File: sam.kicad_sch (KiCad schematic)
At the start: 57 parts, among them IC1 HYB4116, IC15 MC6883, IC16 74LS244, IC2 HYB4116, IC3 HYB4116, IC31 74LS02, IC33 74LS138, IC4 HYB4116, IC5 HYB4116, IC6 HYB4116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

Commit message: validate component values
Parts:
- removed C10, C11, C37: 4.7uF, Capacitor_THT:C_Disc_D3.0mm_W2.0mm_P2.50mm, symbol Device:C_Small
- removed C13: 10uF, Capacitor_THT:C_Disc_D3.0mm_W2.0mm_P2.50mm, symbol Device:C_Small
- added C10, C11, C37: 4.7uF, Capacitor_THT:CP_Radial_D5.0mm_P2.50mm, symbol Device:C_Polarized_Small
- added C13: 10uF, Capacitor_THT:CP_Radial_D5.0mm_P2.50mm, symbol Device:C_Polarized_Small
- C12, C14, C15, C16, C17, C18, C19, C20, C21: footprint Capacitor_THT:C_Disc_D3.0mm_W2.0mm_P2.50mm -> Capacitor_THT:C_Disc_D4.3mm_W1.9mm_P5.00mm
- C50, C51, C52, C53, C54, C55, C56, C57: footprint Capacitor_THT:C_Disc_D3.0mm_W2.0mm_P2.50mm -> Capacitor_THT:C_Disc_D4.7mm_W2.5mm_P5.00mm
- C58: value 0.1uF -> 0.01uF; footprint Capacitor_THT:C_Disc_D3.0mm_W2.0mm_P2.50mm -> Capacitor_THT:C_Disc_D4.3mm_W1.9mm_P5.00mm
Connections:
- net +5V: now also C13.1, C37.1
- net -5V: now also C10.2
- net GND: now also C10.1, C11.2, C13.2, C37.2
- net RAM VDD: now also C11.1

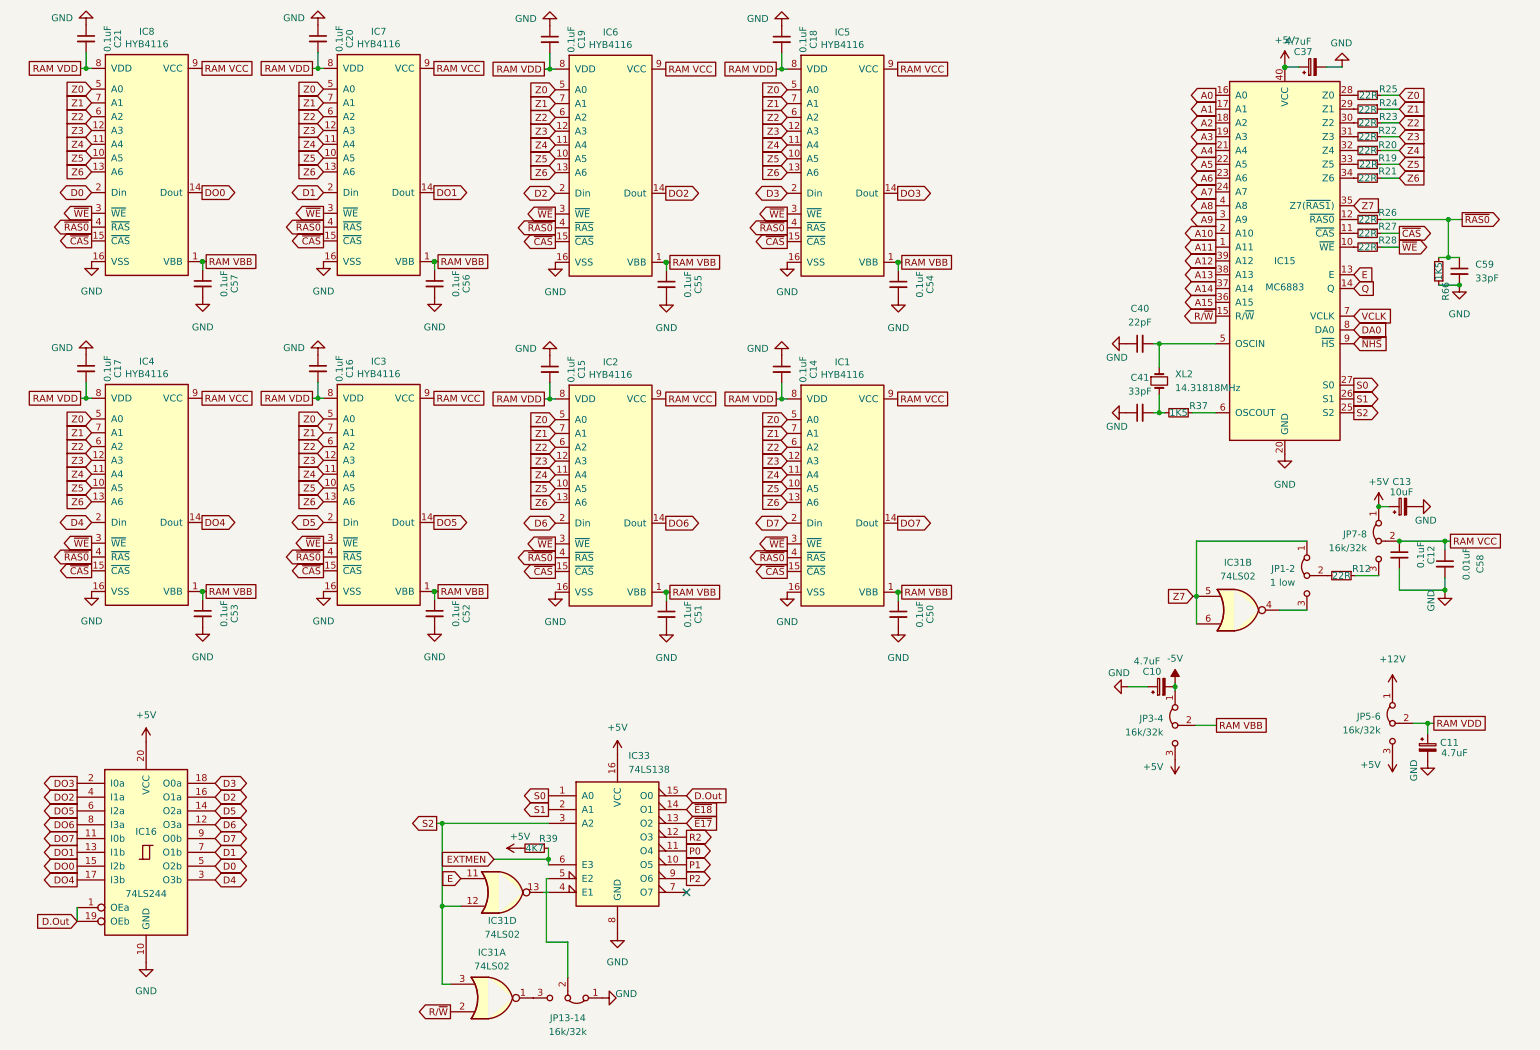
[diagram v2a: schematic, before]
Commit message: cross-reference items to suppliers
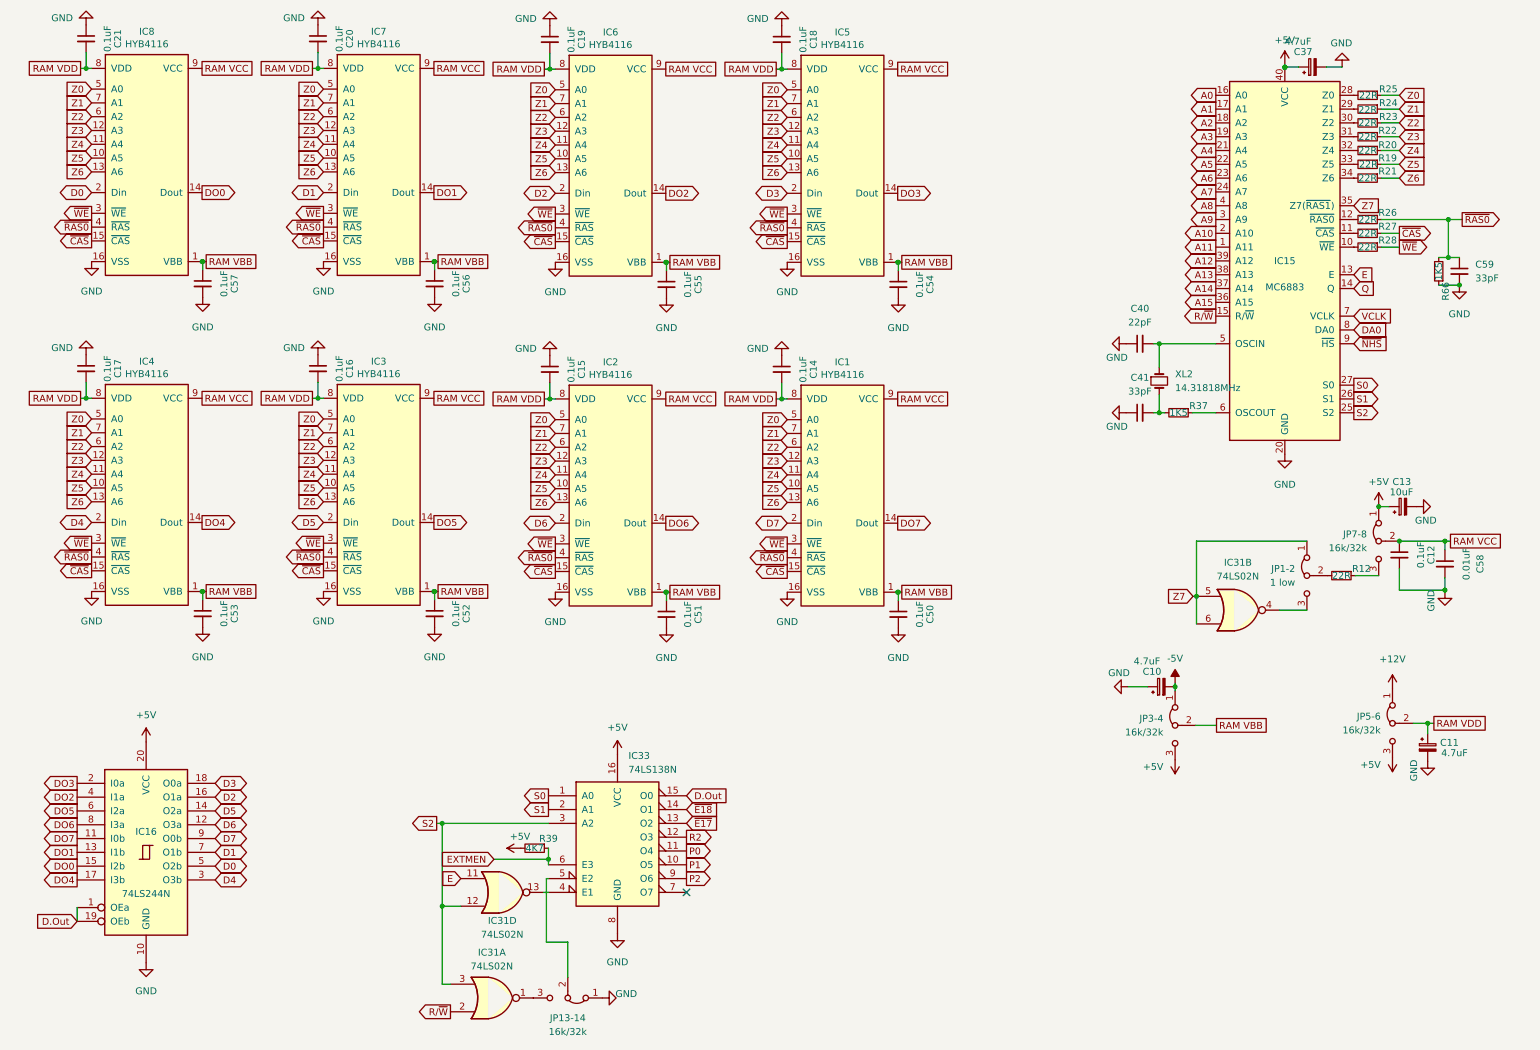
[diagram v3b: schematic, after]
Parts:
- IC16: value 74LS244 -> 74LS244N
- IC31: value 74LS02 -> 74LS02N
- IC33: value 74LS138 -> 74LS138N; DigiKey (none) -> 296-1639-5-ND
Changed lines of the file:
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@@
     (in_bom yes) (on_board yes)
     (property "Reference" "IC16" (id 0) (at 35.306 165.1 0))
-    (property "Value" "74LS244" (id 1) (at 35.306 176.53 0))
+    (property "Value" "74LS244N" (id 1) (at 35.306 176.53 0))
     (property "Footprint" "Package_DIP:DIP-20_W7.62mm" (id 2) (at 35.306 168.91 0)
       (effects (font (size 1.27 1.27)) hide)
@@
     (in_bom yes) (on_board yes)
     (property "Reference" "IC31" (id 0) (at 100.838 181.483 0))
-    (property "Value" "74LS02" (id 1) (at 100.838 184.023 0))
+    (property "Value" "74LS02N" (id 1) (at 100.838 184.023 0))
     (property "Footprint" "Package_DIP:DIP-14_W7.62mm" (id 2) (at 100.838 176.276 0)
       (effects (font (size 1.27 1.27)) hide)
@@
       (effects (font (size 1.27 1.27)) (justify left))
     )
-    (property "Value" "74LS138" (id 1) (at 124.0664 153.67 0)
+    (property "Value" "74LS138N" (id 1) (at 124.0664 153.67 0)
       (effects (font (size 1.27 1.27)) (justify left))
     )
@@
     )
     (property "Datasheet" "http://www.ti.com/lit/gpn/sn74LS138" (id 3) (at 122.047 166.116 0)
+      (effects (font (size 1.27 1.27)) hide)
+    )
+    (property "DigiKey" "296-1639-5-ND" (id 4) (at 122.047 166.116 0)
       (effects (font (size 1.27 1.27)) hide)
     )
@@
     (in_bom yes) (on_board yes) (fields_autoplaced)
     (property "Reference" "IC31" (id 0) (at 236.22 115.57 0))
-    (property "Value" "74LS02" (id 1) (at 236.22 118.11 0))
+    (property "Value" "74LS02N" (id 1) (at 236.22 118.11 0))
     (property "Footprint" "Package_DIP:DIP-14_W7.62mm" (id 2) (at 236.22 124.333 0)
       (effects (font (size 1.27 1.27)) hide)
@@
     (in_bom yes) (on_board yes) (fields_autoplaced)
     (property "Reference" "IC31" (id 0) (at 98.933 187.325 0))
-    (property "Value" "74LS02" (id 1) (at 98.933 189.865 0))
+    (property "Value" "74LS02N" (id 1) (at 98.933 189.865 0))
     (property "Footprint" "Package_DIP:DIP-14_W7.62mm" (id 2) (at 98.933 195.707 0)
       (effects (font (size 1.27 1.27)) hide)

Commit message: update part numbers
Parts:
- C12, C14, C15, C16, C17, C18, C19, C20, C21: DigiKey (none) -> BC1101CT-ND
- C13: DigiKey 399-ESK106M016AC3KACT-ND -> 732-8593-1-ND
- C40: DigiKey (none) -> 399-13930-1-ND
- C41, C59: DigiKey (none) -> BC1007CT-ND
- C50, C51, C52, C53, C54, C55, C56, C57: footprint Capacitor_THT:C_Disc_D4.7mm_W2.5mm_P5.00mm -> Capacitor_THT:C_Disc_D4.3mm_W1.9mm_P5.00mm; DigiKey (none) -> BC1101CT-ND
- C58: DigiKey (none) -> BC2662CT-ND
- IC1, IC2, IC3, IC4, IC5, IC6, IC7, IC8: Note (none) -> use general 4164 with suitable timing
- IC15: Note (none) -> donor
- IC16: DigiKey (none) -> 296-1653-5-ND
- IC31: DigiKey (none) -> 296-1627-5-ND
- XL2: footprint Crystal:Crystal_HC18-U_Horizontal -> Crystal:Crystal_HC49-U_Horizontal; DigiKey (none) -> CTX088-ND

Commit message: resolve part numbers
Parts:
- JP1-2: DigiKey (none) -> 952-2521-ND
- R12, R19, R20, R21, R22, R23, R24, R25, R26, R27, R28: DigiKey (none) -> CF14JT22R0CT-ND
- R37, R66: DigiKey (none) -> CF14JT1K50CT-ND
- R39: DigiKey (none) -> CF14JT4K70CT-ND
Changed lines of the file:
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@@
+      (effects (font (size 1.27 1.27)) hide)
+    )
+    (property "DigiKey" "CF14JT22R0CT-ND" (id 4) (at 260.096 42.291 0)
       (effects (font (size 1.27 1.27)) hide)
     )
@@
       (effects (font (size 1.27 1.27)) hide)
     )
+    (property "DigiKey" "CF14JT22R0CT-ND" (id 4) (at 260.096 54.991 0)
+      (effects (font (size 1.27 1.27)) hide)
+    )
     (pin "1")
     (pin "2")
@@
       (effects (font (size 1.27 1.27)) hide)
     )
+    (pin "1")
+    (pin "2")
+    (pin "3")
+    (pin "4")
+    (pin "5")
+    (pin "6")
+    (pin "10")
+    (pin "8")
+    (pin "9")
     (pin "11")
     (pin "12")
     (pin "13")
+    (pin "14")
+    (pin "7")
   )
   (symbol (lib_id "power:GND") (at 88.392 127.508 0) (unit 1)
@@
       (effects (font (size 1.27 1.27)) hide)
     )
+    (property "DigiKey" "CF14JT1K50CT-ND" (id 4) (at 225.298 88.011 0)
+      (effects (font (size 1.27 1.27)) hide)
+    )
     (pin "1")
     (pin "2")
@@
       (effects (font (size 1.27 1.27)) hide)
     )
+    (pin "1")
+    (pin "2")
+    (pin "3")
     (pin "4")
     (pin "5")
     (pin "6")
+    (pin "10")
+    (pin "8")
+    (pin "9")
+    (pin "11")
+    (pin "12")
+    (pin "13")
+    (pin "14")
+    (pin "7")
   )
   (symbol (lib_id "power:GND") (at 216.027 138.43 270) (mirror x) (unit 1)
@@
       (effects (font (size 1.27 1.27)) hide)
     )
+    (property "DigiKey" "CF14JT4K70CT-ND" (id 4) (at 106.807 168.148 0)
+      (effects (font (size 1.27 1.27)) hide)
+    )
     (pin "1")
     (pin "2")
@@
     (pin "2")
     (pin "3")
+    (pin "4")
+    (pin "5")
+    (pin "6")
+    (pin "10")
+    (pin "8")
+    (pin "9")
+    (pin "11")
+    (pin "12")
+    (pin "13")
+    (pin "14")
+    (pin "7")
   )
   (symbol (lib_id "Memory_RAM_Siemens:HYB4116") (at 120.777 103.251 0) (unit 1)
@@
       (effects (font (size 1.27 1.27)) hide)
     )
+    (property "DigiKey" "CF14JT22R0CT-ND" (id 4) (at 260.096 34.671 0)
+      (effects (font (size 1.27 1.27)) hide)
+    )
     (pin "1")
     (pin "2")
@@
       (effects (font (size 1.27 1.27)) hide)
     )
+    (property "DigiKey" "CF14JT22R0CT-ND" (id 4) (at 260.096 52.451 0)
+      (effects (font (size 1.27 1.27)) hide)
+    )
     (pin "1")
     (pin "2")
@@
       (effects (font (size 1.27 1.27)) hide)
     )
+    (property "DigiKey" "CF14JT1K50CT-ND" (id 4) (at 273.177 61.976 0)
+      (effects (font (size 1.27 1.27)) hide)
+    )
     (pin "1")
     (pin "2")
@@
       (effects (font (size 1.27 1.27)) hide)
     )
+    (property "DigiKey" "CF14JT22R0CT-ND" (id 4) (at 260.096 29.591 0)
+      (effects (font (size 1.27 1.27)) hide)
+    )
     (pin "1")
     (pin "2")
@@
     )
     (property "Datasheet" "~" (id 3) (at 248.92 117.983 0)
+      (effects (font (size 1.27 1.27)) hide)
+    )
+    (property "DigiKey" "952-2521-ND" (id 4) (at 248.92 117.983 0)
       (effects (font (size 1.27 1.27)) hide)
     )
@@
       (effects (font (size 1.27 1.27)) hide)
     )
+    (property "DigiKey" "CF14JT22R0CT-ND" (id 4) (at 255.27 117.983 0)
+      (effects (font (size 1.27 1.27)) hide)
+    )
     (pin "1")
     (pin "2")
@@
       (effects (font (size 1.27 1.27)) hide)
     )
+    (property "DigiKey" "CF14JT22R0CT-ND" (id 4) (at 260.096 37.211 0)
+      (effects (font (size 1.27 1.27)) hide)
+    )
     (pin "1")
     (pin "2")
@@
     )
     (property "Datasheet" "~" (id 3) (at 260.096 44.831 0)
+      (effects (font (size 1.27 1.27)) hide)
+    )
+    (property "DigiKey" "CF14JT22R0CT-ND" (id 4) (at 260.096 44.831 0)
       (effects (font (size 1.27 1.27)) hide)
     )
@@
       (effects (font (size 1.27 1.27)) hide)
     )
+    (property "DigiKey" "CF14JT22R0CT-ND" (id 4) (at 260.096 32.131 0)
+      (effects (font (size 1.27 1.27)) hide)
+    )
     (pin "1")
     (pin "2")
@@
     )
     (property "Datasheet" "~" (id 3) (at 260.096 39.751 0)
+      (effects (font (size 1.27 1.27)) hide)
+    )
+    (property "DigiKey" "CF14JT22R0CT-ND" (id 4) (at 260.096 39.751 0)
       (effects (font (size 1.27 1.27)) hide)
     )
@@
       (effects (font (size 1.27 1.27)) hide)
     )
+    (property "DigiKey" "CF14JT22R0CT-ND" (id 4) (at 260.096 57.531 0)
+      (effects (font (size 1.27 1.27)) hide)
+    )
